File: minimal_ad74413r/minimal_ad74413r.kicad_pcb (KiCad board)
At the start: 4 copper layers, 48.3 x 42.5 mm, 104 parts, among them J1 FW-02-03-G-D-085-155, J2 FW-02-03-G-D-085-155, J3 FW-02-03-G-D-085-155, J4 FW-02-03-G-D-085-155, J5 FW-02-03-G-D-085-155, J6 FW-02-03-G-D-085-155, J7 FW-14-03-G-D-085-155, Q1 ZXMP6A17E6TA, Q2 ZXMP6A17E6TA, Q3 ZXMP6A17E6TA, Q4 ZXMP6A17E6TA, U1 AD74413RBCPZ

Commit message: Update subproject commit for KiCAD_Symbol_Generator
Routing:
- net /GPO_A: track 36.7 -> 35.9 mm
- net /GPO_B: track 35.8 -> 35.0 mm
- net /GPO_D: track 37.8 -> 37.0 mm
- net /GPO_C: track 40.5 -> 39.8 mm

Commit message: Update footprint library URIs to use KiCAD_Symbols_Generator
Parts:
- C1, C17, C18, C2: value 10 uF -> 10 µF
- C12, C13, C21, C22, C25, C26, C27, C28, C6, C7, C8, C9: value 0.01 uF -> 10 nF
- C14, C16, C19, C20, C29, C3, C30, C31, C5: value 0.1uF -> 100 nF
- C15, C32: value 2.2 uF -> 2.2 µF
- C4: value 0.33 uF -> 330 nF
- CR1, CR2, CR3, CR4: value SBAV99WT1G -> 100 V
- Q1, Q2, Q3, Q4: value ZXMP6A17E6TA -> -60 V
- R1, R13, R14, R19, R2, R20, R7, R8: value 2k -> 2 kΩ
- R10, R11, R12, R17, R18, R3, R4, R9: value 10k -> 10 kΩ
- R15, R16, R5, R6: value 100 -> 100 Ω

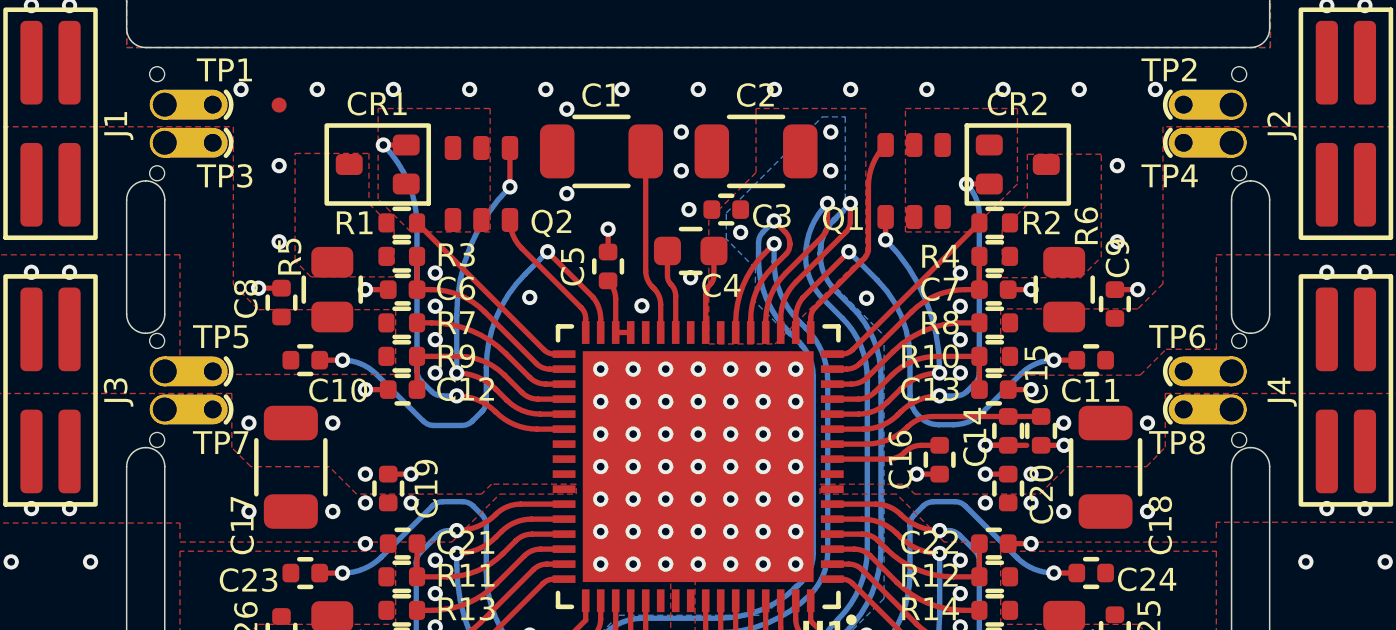
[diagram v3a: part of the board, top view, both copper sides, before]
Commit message: Add top image and update dimensions in KiCAD project for minimal_ad74413r
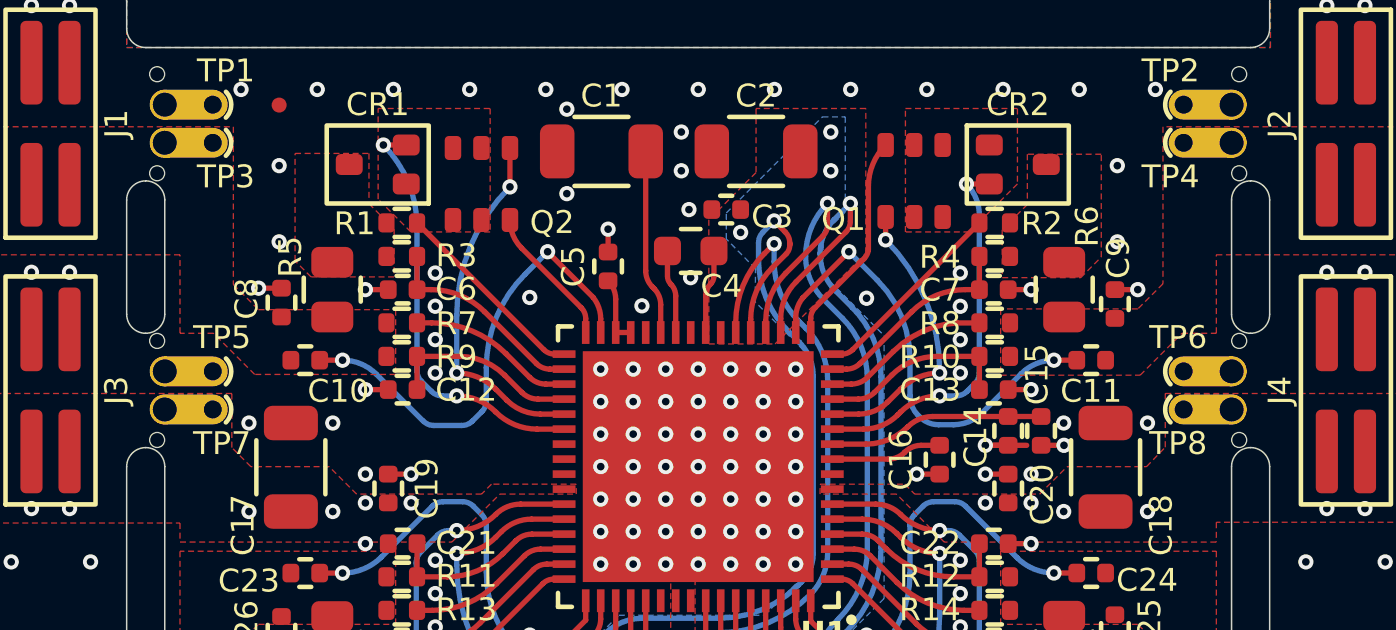
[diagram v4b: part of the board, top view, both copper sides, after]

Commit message: Development backup
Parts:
- moved MB7 1.91 mm to (151.8, 118.0)
- moved TP13 1.91 mm to (143.5, 117.5)
- moved TP14 1.91 mm to (144.8, 117.5)
- moved TP15 1.91 mm to (146.1, 117.5)
- moved TP16 1.91 mm to (147.3, 117.5)
- moved TP17 1.91 mm to (148.6, 117.5)
- moved TP18 1.91 mm to (149.9, 117.5)
- moved TP19 1.91 mm to (151.1, 117.5)
- moved TP20 1.91 mm to (152.4, 117.5)
- moved TP21 1.91 mm to (153.7, 117.5)
- moved TP22 1.91 mm to (154.9, 117.5)
- moved TP23 1.91 mm to (156.2, 117.5)
- moved TP24 1.91 mm to (157.5, 117.5)
- moved TP25 1.91 mm to (158.8, 117.5)
- moved TP26 1.91 mm to (160.0, 117.5)
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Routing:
- net /GPO_D: track 37.0 -> 35.1 mm
- net /~{RESET}: track 14.6 -> 12.7 mm
- net /SDO: track 14.6 -> 12.7 mm
- net /~{LDAC}: track 14.4 -> 12.5 mm
- net /SCLK: track 14.2 -> 12.3 mm
- net /GPO_A: track 35.9 -> 34.0 mm
- net /GPO_C: track 39.8 -> 37.9 mm
- net /GPO_B: track 35.0 -> 33.1 mm
- net GNDA: vias 191 -> 178
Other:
- board size 48.3 x 42.5 mm -> 48.3 x 40.6 mm

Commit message: Development backup
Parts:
- added D12: 40 V, diode_footprints:DO-214AB-2, F.Cu at (169.5, 112.3)
- added D13: 40 V, diode_footprints:DO-214AB-2, F.Cu at (169.5, 93.5)
- added D14: 40 V, diode_footprints:DO-214AB-2, F.Cu at (134.1, 93.5)
- added D15: 40 V, diode_footprints:DO-214AB-2, F.Cu at (134.1, 112.3)
- moved TP1 6.35 mm to (127.6, 90.8)
- moved TP11 6.35 mm to (127.6, 114.9)
- moved TP3 6.35 mm to (127.6, 92.1)
- moved TP5 6.35 mm to (127.6, 99.7)
- moved TP7 6.35 mm to (127.6, 101.0)
- moved TP9 6.35 mm to (127.6, 113.7)
- moved J1 6.35 mm to (123.8, 91.4)
- moved J2 6.35 mm to (179.7, 91.4)
- moved J3 6.35 mm to (123.8, 100.3)
- moved J4 6.35 mm to (179.7, 100.3)
- moved J5 6.35 mm to (123.8, 114.3)
- moved J6 6.35 mm to (179.7, 114.3)
- moved MB1 6.35 mm to (127.0, 91.4)
- moved MB2 6.35 mm to (176.5, 91.4)
- moved MB3 6.35 mm to (127.0, 100.3)
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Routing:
- net GNDA: vias 178 -> 174
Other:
- board size 48.3 x 40.6 mm -> 61 x 40.6 mm
